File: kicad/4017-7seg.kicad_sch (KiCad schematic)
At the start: 36 parts, among them U2 D168K, U3 4017

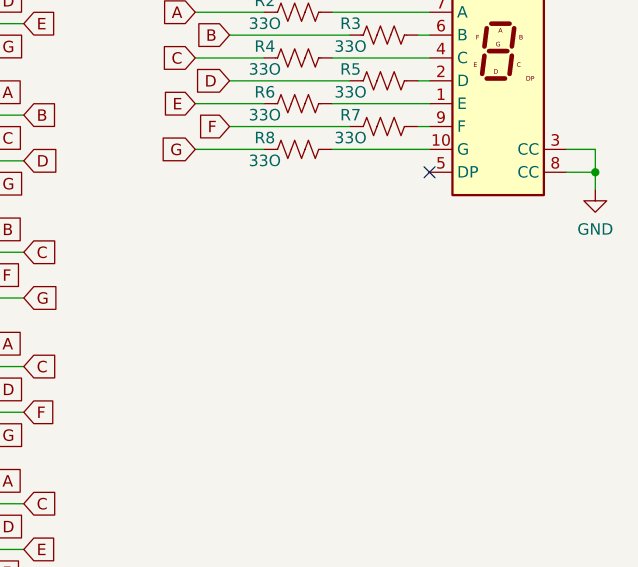
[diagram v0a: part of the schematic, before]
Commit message: Consider 4017->4511->7seg
Promising, if untested
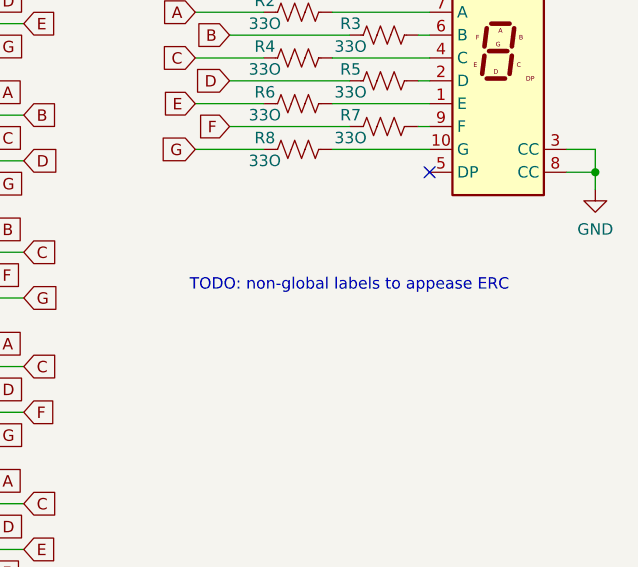
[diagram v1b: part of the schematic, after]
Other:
- note added: "TODO: non-global labels to appease ERC"
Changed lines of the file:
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@@
     (stroke (width 0) (type default) (color 0 0 0 0))
+  )
+  (text "TODO: non-global labels to appease ERC" (at 180.975 107.315 0)
+    (effects (font (size 1.27 1.27)) (justify left bottom))
   )
   (global_label "D" (shape input) (at 158.75 74.93 0) (fields_autoplaced)

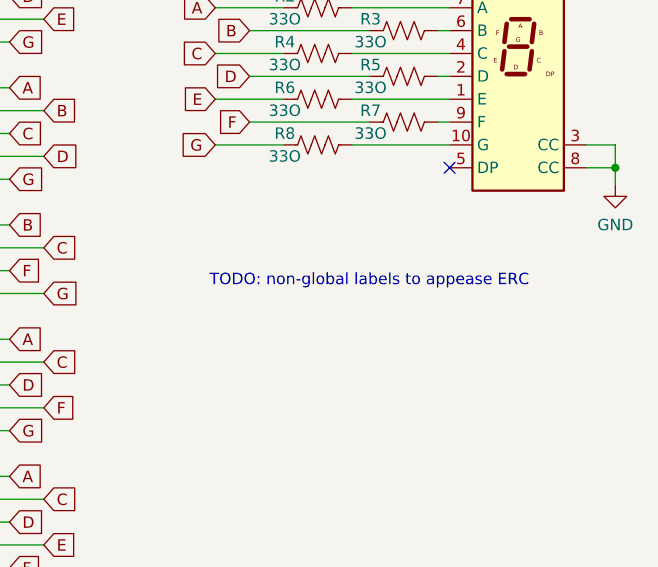
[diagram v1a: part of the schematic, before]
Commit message: Note BOM effects in different implementations
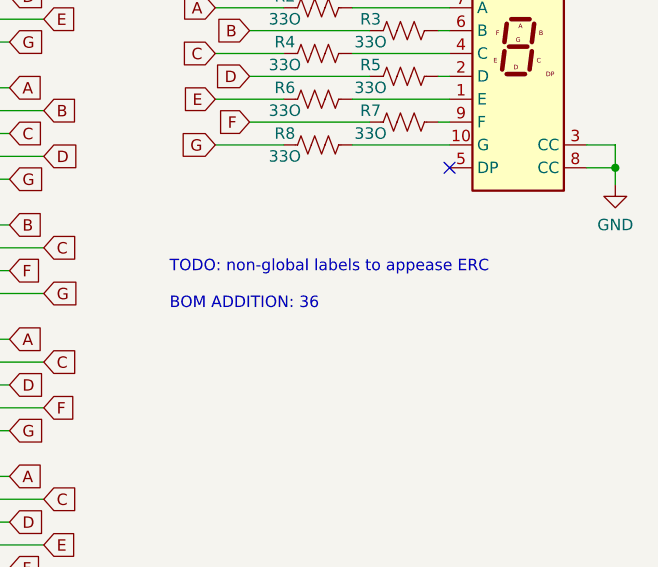
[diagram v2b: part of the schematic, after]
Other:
- note added: "TODO: non-global labels to appease ERC BOM ADDITION: 36"
- note removed: "TODO: non-global labels to appease ERC"
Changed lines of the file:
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@@
     (stroke (width 0) (type default) (color 0 0 0 0))
   )
-  (text "TODO: non-global labels to appease ERC" (at 180.975 107.315 0)
+  (text "TODO: non-global labels to appease ERC\n\nBOM ADDITION: 36"
+    (at 176.53 109.855 0)
     (effects (font (size 1.27 1.27)) (justify left bottom))
   )

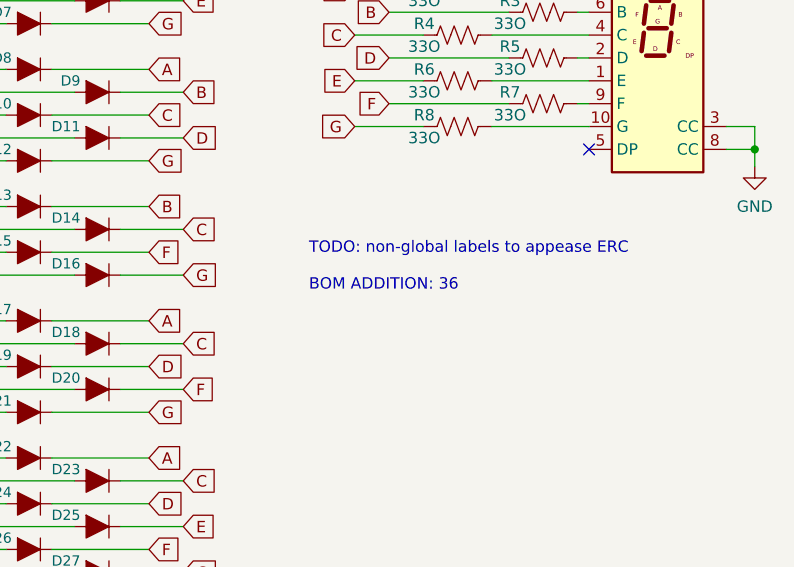
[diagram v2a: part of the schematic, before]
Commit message: Hmmm, may need resistors for LED driver ICs
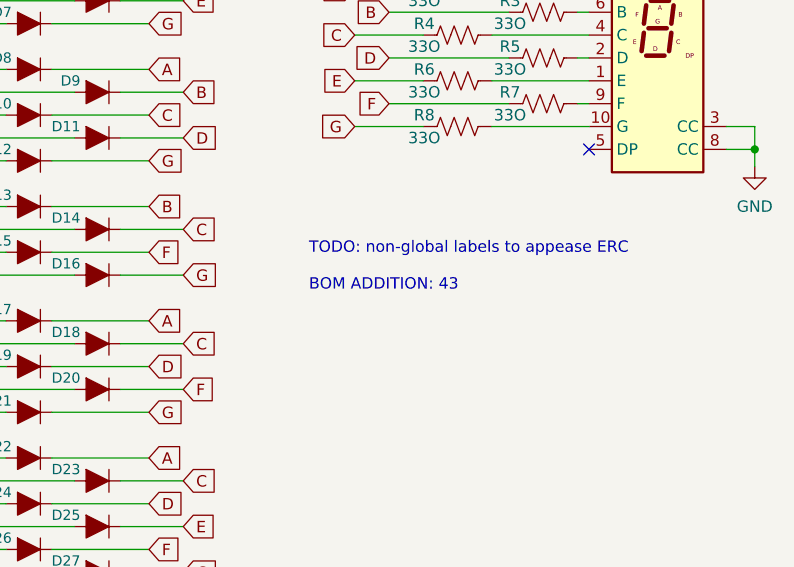
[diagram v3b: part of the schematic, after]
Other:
- note added: "TODO: non-global labels to appease ERC BOM ADDITION: 43"
- note removed: "TODO: non-global labels to appease ERC BOM ADDITION: 36"
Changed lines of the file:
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@@
     (stroke (width 0) (type default) (color 0 0 0 0))
   )
-  (text "TODO: non-global labels to appease ERC\n\nBOM ADDITION: 36"
+  (text "TODO: non-global labels to appease ERC\n\nBOM ADDITION: 43"
     (at 176.53 109.855 0)
     (effects (font (size 1.27 1.27)) (justify left bottom))

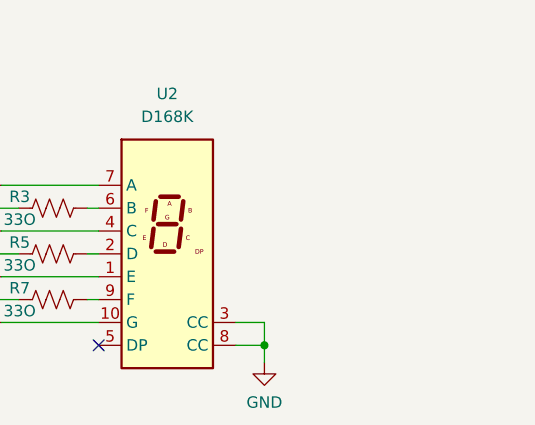
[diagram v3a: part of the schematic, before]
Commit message: TODO: fix 7seg footprint
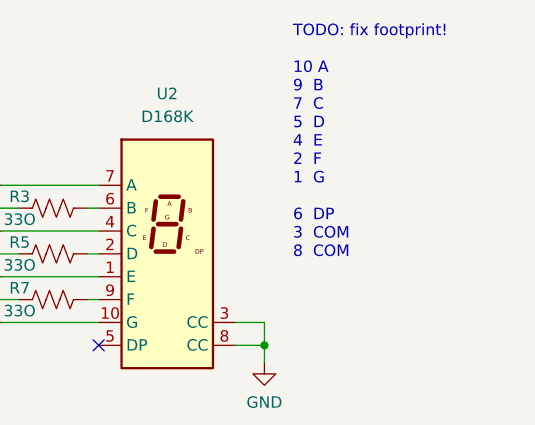
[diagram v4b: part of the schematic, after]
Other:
- note added: "TODO: fix footprint! 10 A 9 B 7 C 5 D 4 E 2 F 1 G 6 DP 3 COM 8 COM"
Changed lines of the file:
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@@
+    (effects (font (size 1.27 1.27)) (justify left bottom))
+  )
+  (text "TODO: fix footprint!\n\n10 A\n9  B\n7  C\n5  D\n4  E\n2  F\n1  G\n\n6  DP\n3  COM\n8  COM"
+    (at 229.235 84.455 0)
     (effects (font (size 1.27 1.27)) (justify left bottom))
   )

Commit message: Fix 7seg footprint
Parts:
- removed U2: D168K, Display_7Segment:D1X8K, symbol Display_Character:D168K
- added U2: TDSR-3163-G, symbol parts_cafe:TDSR-3163-G
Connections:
- net GND: now also U2.3 (CC), U2.8 (CC)
- net at R6.2: now also U2.4 (E)
- net at R8.2: now also U2.1 (G)
- net at R5.2: now also U2.5 (D)
- net at R4.2: now also U2.7 (C)
- net at R3.2: now also U2.9 (B)
- net at R2.2: now also U2.10 (A)
- net at R7.2: now also U2.2 (F)
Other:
- note removed: "TODO: fix footprint! 10 A 9 B 7 C 5 D 4 E 2 F 1 G 6 DP 3 COM 8 COM"
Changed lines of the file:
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@@
-    (effects (font (size 1.27 1.27)) (justify left bottom))
-  )
-  (text "TODO: fix footprint!\n\n10 A\n9  B\n7  C\n5  D\n4  E\n2  F\n1  G\n\n6  DP\n3  COM\n8  COM"
-    (at 229.235 84.455 0)
     (effects (font (size 1.27 1.27)) (justify left bottom))
   )
@@
     (pin "A")
     (pin "C")
-  )
-  (symbol (lib_id "Display_Character:D168K") (at 215.265 83.82 0) (unit 1)
-    (in_bom yes) (on_board yes) (fields_autoplaced)
-    (property "Reference" "U2" (id 0) (at 215.265 66.04 0))
-    (property "Value" "D168K" (id 1) (at 215.265 68.58 0))
-    (property "Footprint" "Display_7Segment:D1X8K" (id 2) (at 215.265 99.06 0)
-      (effects (font (size 1.27 1.27)) hide)
-    )
-    (property "Datasheet" "https://ia800903.us.archive.org/24/items/CTKD1x8K/Cromatek%20D168K.pdf" (id 3) (at 202.565 71.755 0)
-      (effects (font (size 1.27 1.27)) (justify left) hide)
-    )
-    (pin "1")
-    (pin "10")
-    (pin "2")
-    (pin "3")
-    (pin "4")
-    (pin "5")
-    (pin "6")
-    (pin "7")
-    (pin "8")
-    (pin "9")
   )
   (symbol (lib_id "SparkFun-DiscreteSemi:DIODE-1N4148") (at 153.035 92.71 0) (unit 1)
@@
     (pin "1")
   )
+  (symbol (lib_id "parts_cafe:TDSR-3163-G") (at 210.185 69.85 0) (unit 1)
+    (in_bom yes) (on_board yes) (fields_autoplaced)
+    (property "Reference" "U2" (id 0) (at 215.265 65.405 0))
+    (property "Value" "TDSR-3163-G" (id 1) (at 215.265 67.945 0))
+    (property "Footprint" "" (id 2) (at 210.185 69.85 0)
+      (effects (font (size 1.27 1.27)) hide)
+    )
+    (property "Datasheet" "" (id 3) (at 210.185 69.85 0)
+      (effects (font (size 1.27 1.27)) hide)
+    )
+    (pin "1")
+    (pin "10")
+    (pin "2")
+    (pin "3")
+    (pin "4")
+    (pin "5")
+    (pin "6")
+    (pin "7")
+    (pin "8")
+    (pin "9")
+  )
   (symbol (lib_id "SparkFun-DiscreteSemi:DIODE-1N4148") (at 153.035 87.63 0) (unit 1)

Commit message: Update to latest kicad
no functional changes
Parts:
- renumbered D17 to D10, D19 to D11, D21 to D12, D22 to D13, D24 to D14, D26 to D15, D2 to D16, D4 to D17, D6 to D18, D9 to D19, D3 to D2, D11 to D20, D14 to D21, D16 to D22, D18 to D23, D20 to D24, D23 to D25, D25 to D26, D5 to D3, D7 to D4, D8 to D5, D10 to D6, D12 to D7, D13 to D8, D15 to D9, R4 to R3, R6 to R4, R8 to R5, R3 to R6, R5 to R7, R7 to R8, U3 to U2, U2 to U3
